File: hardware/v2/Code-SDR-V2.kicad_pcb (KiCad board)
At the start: 4 copper layers, 99 x 99 mm, 344 parts, among them J1 5V_INPUT_ONLY, J10 USB_B_Micro, J11 Cortex_SWD_10pin, J30 JK0654219NL, J50 RF_LOW_0.1_2.5GHz, J60 RF_HIGH_2.3_4.2GHz, J61 RF_HIGH_4.2_6.8GHz, J62 RF_HIGH_6.8_9.2GHz, J63 RF_HIGH_8.0_10GHz, SW1 BOOTSEL, SW2 RESET, T50 2450BL15B0200001E, T60 TC1-1-13M+, T70 2450BL15B0100001E, U1 TLV62569DBVR, U10 RP2040, U11 W25Q16JVSSIQ, U12 USBLC6-2SC6, U2 TLV62569DBVR, U20 LIF-MD6000-6JMG80I, U21 AD9215BCPZ-105, U3 TLV75525PDBVR, U30 KSZ9031RNXCA, U4 TLV76733DRVR, U40 LMX2592RHAT, U41 ADF4360-1BCPZ, U42 CDCLVC1104PWR, U50 GRF4001, U51 ADL5801ACPZ-R7, U60 GRF4001, U61 GRF2101, U62 GRF2101, U63 LTC5548IUDB, U64 QPC6144TR13, U66 GRF2101, U67 GRF2101, U70 BGS12WN6E6327, U71 GRF2013, U72 PE4312C-Z, U73 LT5560EDD, U74 AD8351ARMZ, U75 GRF2013, Y10 ABM8-272-T3_12MHz, Y30 ECS-250-20-33-TR_25MHz, Y40 SiT8209AC-23-33E-100.000000X

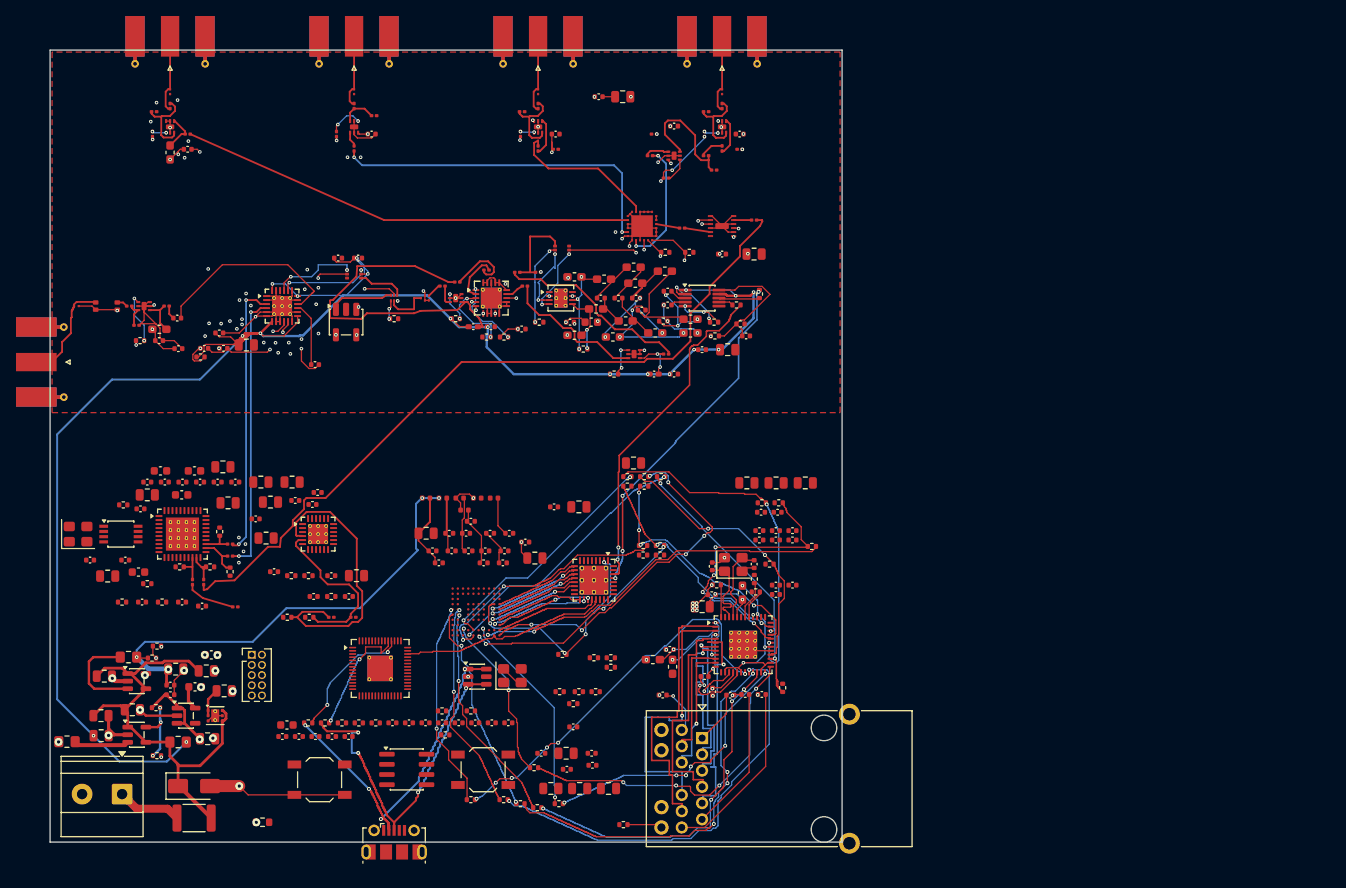
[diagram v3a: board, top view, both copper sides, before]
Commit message: hardware: checkpoint corrected V2 routing at 108 opens
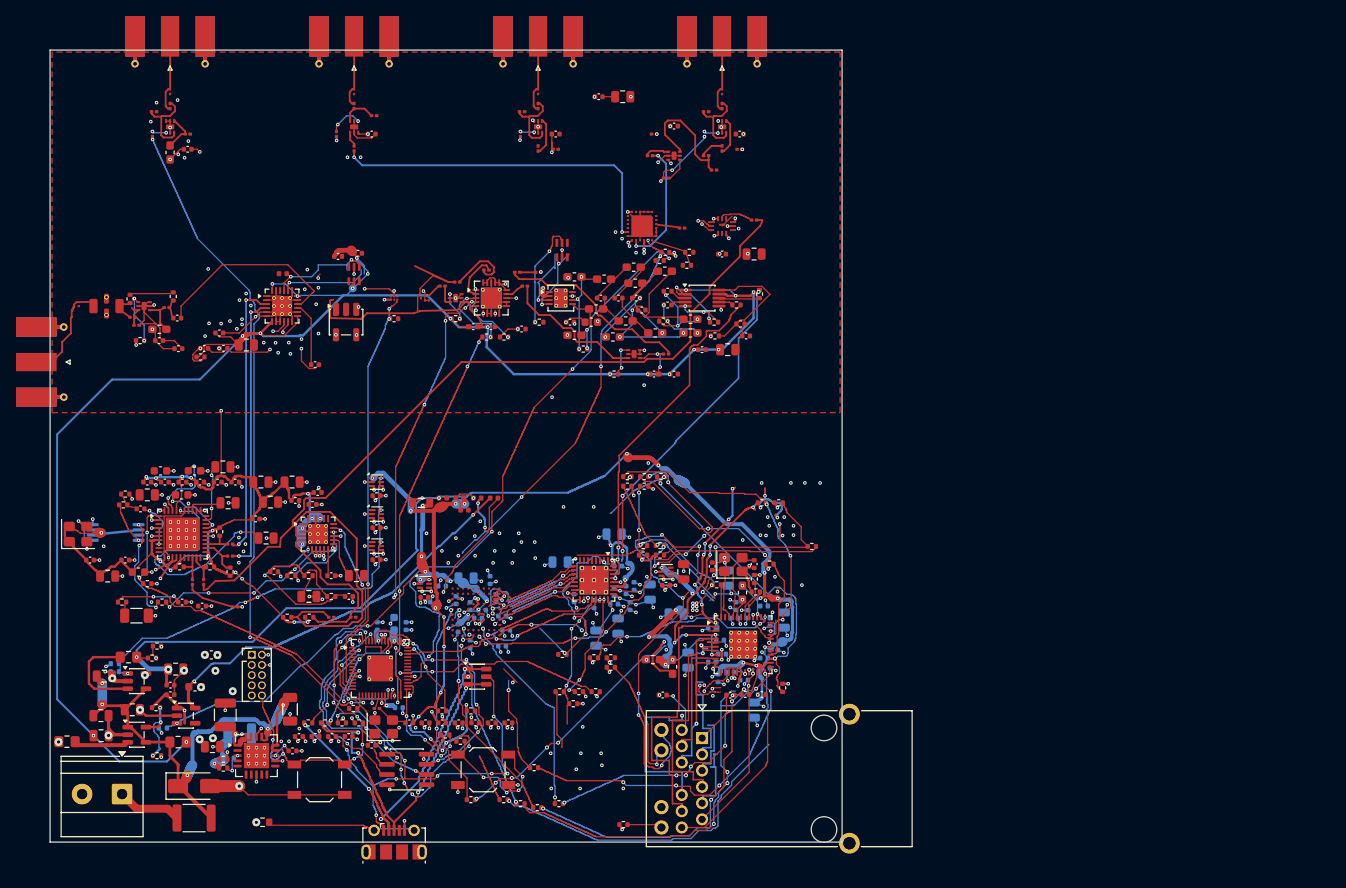
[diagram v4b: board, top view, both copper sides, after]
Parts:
- added C330: 100nF, Capacitor_SMD:C_0402_1005Metric, B.Cu at (43.6, 82.2)
- added C331: 100nF, Capacitor_SMD:C_0402_1005Metric, B.Cu at (40.9, 72.0)
- added C340: 100nF, Capacitor_SMD:C_0402_1005Metric, F.Cu at (40.8, 55.7)
- added C341: 100nF, Capacitor_SMD:C_0402_1005Metric, F.Cu at (40.8, 59.7)
- added C342: 100nF, Capacitor_SMD:C_0402_1005Metric, F.Cu at (40.8, 63.7)
- added C343: 100nF, Capacitor_SMD:C_0402_1005Metric, F.Cu at (46.8, 68.4)
- added C344: 100nF, Capacitor_SMD:C_0402_1005Metric, F.Cu at (77.0, 66.9)
- added C345: 20nF_C0G_5%, Capacitor_SMD:C_0805_2012Metric, F.Cu at (79.2, 65.2)
- added C346: 47uF_10V_X7R, Capacitor_SMD:C_1210_3225Metric, B.Cu at (23.7, 85.5)
- added C347: 100nF, Capacitor_SMD:C_0402_1005Metric, F.Cu at (30.3, 87.6)
- added C348: 10nF, Capacitor_SMD:C_0402_1005Metric, B.Cu at (22.5, 88.5)
- added L98: 2.7nH, Inductor_SMD:L_0402_1005Metric, F.Cu at (29.1, 27.9)
- added R150: 1k, Resistor_SMD:R_0201_0603Metric, F.Cu at (40.9, 82.3)
- added R151: 1k, Resistor_SMD:R_0402_1005Metric, F.Cu at (51.3, 86.4)
- added R152: 150R_1%, Resistor_SMD:R_0402_1005Metric, F.Cu at (9.40, 55.5)
- added R153: 0R, Resistor_SMD:R_0402_1005Metric, F.Cu at (10.0, 31.1)
- added R154: 30.3k_0.1%, Resistor_SMD:R_0402_1005Metric, F.Cu at (21.6, 89.8)
- added R155: 10k_0.1%, Resistor_SMD:R_0402_1005Metric, F.Cu at (21.6, 88.7)
- added R156: 0R, Resistor_SMD:R_0402_1005Metric, F.Cu at (15.4, 30.8)
- added R157: 120k_1%, Resistor_SMD:R_0402_1005Metric, B.Cu at (8.10, 76.7)
- added R158: 100k_1%, Resistor_SMD:R_0402_1005Metric, B.Cu at (8.10, 77.7)
- added R159: 120k_1%, Resistor_SMD:R_0402_1005Metric, B.Cu at (14.1, 84.8)
- added R160: 1k_1%, Resistor_SMD:R_0402_1005Metric, F.Cu at (76.2, 26.3)
- added R161: 1k_1%, Resistor_SMD:R_0402_1005Metric, F.Cu at (79.6, 26.9)
- added U5: TPS389033DSER, Package_SON:WSON-6_1.5x1.5mm_P0.5mm, F.Cu at (40.8, 54.0)
- added U6: TPS389033DSER, Package_SON:WSON-6_1.5x1.5mm_P0.5mm, F.Cu at (40.8, 58.0)
- added U7: TPS389033DSER, Package_SON:WSON-6_1.5x1.5mm_P0.5mm, F.Cu at (40.8, 62.0)
- added U8: TPS389012DSER, Package_SON:WSON-6_1.5x1.5mm_P0.5mm, F.Cu at (46.8, 66.7)
- added U9: TPS389012DSER, Package_SON:WSON-6_1.5x1.5mm_P0.5mm, F.Cu at (77.0, 65.2)
- C11: value 4.7uF -> 22uF_10V_X7R; footprint Capacitor_SMD:C_0805_2012Metric -> Capacitor_SMD:C_1206_3216Metric
- C12: value 4.7uF -> 47uF_10V_X7R; footprint Capacitor_SMD:C_0805_2012Metric -> Capacitor_SMD:C_1210_3225Metric
- C154, C156, C159, C22, C295, C296, C297, C298, C299, C300, C301, C302, C303, C304, C305, C310, C311, C312, C313, C314, C315, C316, C317, C318, C319, C320, C321, C322, C323, C40, C41, C42, C43, C44, C45, C46, C47, C48, C50, C51, C52, C53, C54, C55, C56, C57, C58: moved to B.Cu
- C155: value 10uF -> 100nF; footprint Capacitor_SMD:C_0805_2012Metric -> Capacitor_SMD:C_0402_1005Metric; moved to B.Cu
- C205: value 15nF_C0G -> 470pF_C0G
- C262, C268: value 100pF_C0G -> 51pF_C0G
- C264, C266: value 110pF_C0G -> 56pF_C0G
- C306: value 100nF -> 1uF; moved to B.Cu
- C71: value 100nF -> 100nF_C0G; footprint Capacitor_SMD:C_0402_1005Metric -> Capacitor_SMD:C_1206_3216Metric
- C74: value 1nF_C0G -> 470pF_C0G
- C75: value 3.3nF_C0G -> 22nF_C0G; footprint Capacitor_SMD:C_0402_1005Metric -> Capacitor_SMD:C_0805_2012Metric
- FB33: value 120R@100MHz -> BLM21SN300SN1D; footprint Inductor_SMD:L_0402_1005Metric -> Inductor_SMD:L_0805_2012Metric
- J50: value RF_LOW_0.1_2.5GHz -> RF_LOW_0.01_2.5GHz_OPTION
- R1: value 453k_1% -> 453k_0.1%
- R144, R145: value 100k -> 10k_1%
- R2, R4: value 100k_1% -> 100k_0.1%
- R3: value 100k_1% -> 101k_0.1%
- R50: value 33R -> 150R_1%
- R56: value 68R_1% -> 220R_1%
- R59: value 620R_1% -> 1k_1%
- R93: value 51R -> 220R_1%
- U11: value W25Q16JVSSIQ -> W25Q16JVSNIQ
- U4: value TLV76733DRVR -> TPS7A8300ARGWT; footprint Package_SON:WSON-6-1EP_2x2mm_P0.65mm_EP1x1.6mm_ThermalVias -> Package_DFN_QFN:Texas_RGW0020A_VQFN-20-1EP_5x5mm_P0.65mm_EP3.15x3.15mm_ThermalVias
- U42: footprint Package_SO:TSSOP-8_3x3mm_P0.65mm -> Package_SO:TSSOP-8_4.4x3mm_P0.65mm; moved to B.Cu
- moved C57 34.4 mm to (88.0, 82.5), turned to -90 degrees
- moved C154 26.1 mm to (75.0, 67.8), turned to -90 degrees
- moved C300 24.7 mm to (79.8, 76.2), turned to -90 degrees
- moved C155 24.6 mm to (70.5, 67.8), turned to -90 degrees
- moved C48 23.0 mm to (73.0, 67.0), turned to 90 degrees
- moved C44 23.0 mm to (72.0, 67.5), turned to -90 degrees
- moved C46 21.5 mm to (70.5, 69.2)
- moved C306 20.7 mm to (44.5, 72.0), turned to 90 degrees
- moved C159 19.6 mm to (68.2, 73.5), turned to -90 degrees
- moved C299 19.0 mm to (84.0, 75.5)
- moved C47 19.0 mm to (72.5, 69.5), turned to -90 degrees
- moved C52 18.7 mm to (83.5, 78.5), turned to -90 degrees
- moved C297 18.6 mm to (78.2, 70.5), turned to 180 degrees
- moved C53 18.5 mm to (86.8, 78.8)
- moved C22 18.4 mm to (43.0, 71.7), turned to 90 degrees
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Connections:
- C154 pad 1: ADC_REFB -> ADC_REFT
- C154 pad 2: GND -> ADC_REFB
- C155 pad 2: GND -> ADC_REFB
- C70 pad 1: LMX_CPOUT -> LMX_VTUNE
- C71 pad 1: LMX_VTUNE -> LMX_LF_DAMP
- R144 pad 1: HSW_V1 -> HSW_V1_CHIP
- R145 pad 1: HSW_V2 -> HSW_V2_CHIP
- R56 pad 1: LMX_CPOUT -> LMX_VTUNE
- R56 pad 2: LMX_VTUNE -> LMX_LF_DAMP
- R93 pad 1: ADF_LF1 -> ADF_CPOUT
- SW1 pad 1: QSPI_SS_N -> BOOTSEL_SWITCH
- U10 pad 21: RP_XOUT -> RP_XOUT_DRIVE
- U2 pad 1: VIN_FUSED -> CORE_EN
- U3 pad 3: +3V3_DIG -> AUX_EN
- U4 pad 2: +3V3_ANA -> (no net)
- U4 pad 3: GND -> FB_ANA
- U4 pad 4: VIN_FUSED -> (no net)
- U4 pad 5: GND -> (no net)
- U4 pad 6: VIN_FUSED -> (no net)
- U4 pad 7: GND -> (no net)
- U40 pad 12: LMX_CPOUT -> LMX_VTUNE
- U64 pad 17: HSW_V1 -> HSW_V1_CHIP
- U64 pad 18: HSW_V2 -> HSW_V2_CHIP
- U73 pad 2: +3V3_DIG -> +3V3_ANA
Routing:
- net +3V3_ANA: track 21.5 -> 149.0 mm, vias 23 -> 52
- net LNA_EN_H1: track 0.37 -> 87.0 mm, vias 1 -> 4
- net +1V2_CORE: track 81.5 -> 162.6 mm, vias 8 -> 19
- net HSW_V1: track 2.77 -> 75.9 mm, vias 1 -> 4
- net GND: track 202.4 -> 266.6 mm, vias 84 -> 300
- net USB_VBUS_SENSE: track 0.00 -> 58.0 mm, vias 0 -> 9
- net IF_PATH_SEL: track 2.47 -> 59.9 mm, vias 2 -> 7
- net RF_HA_LNA_OUT: track 57.0 -> 0.00 mm
- net PHY_LED2: track 11.7 -> 68.0 mm, vias 1 -> 8
- net DSA_CLK: track 0.52 -> 56.2 mm, vias 1 -> 8
- net FPGA_VCCIO0_3V3: track 6.88 -> 62.3 mm, vias 0 -> 15
- net DSA_DATA: track 0.00 -> 50.4 mm, vias 0 -> 4
- net CORE_EN: track 0.00 -> 50.3 mm, vias 0 -> 6
- net HSW_V1_CHIP: track 0.00 -> 49.8 mm, vias 0 -> 4
- net +2V5_AUX: track 3.02 -> 49.5 mm, vias 0 -> 2
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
